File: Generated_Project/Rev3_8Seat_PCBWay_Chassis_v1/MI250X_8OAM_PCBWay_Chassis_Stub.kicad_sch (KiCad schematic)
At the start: 0 parts

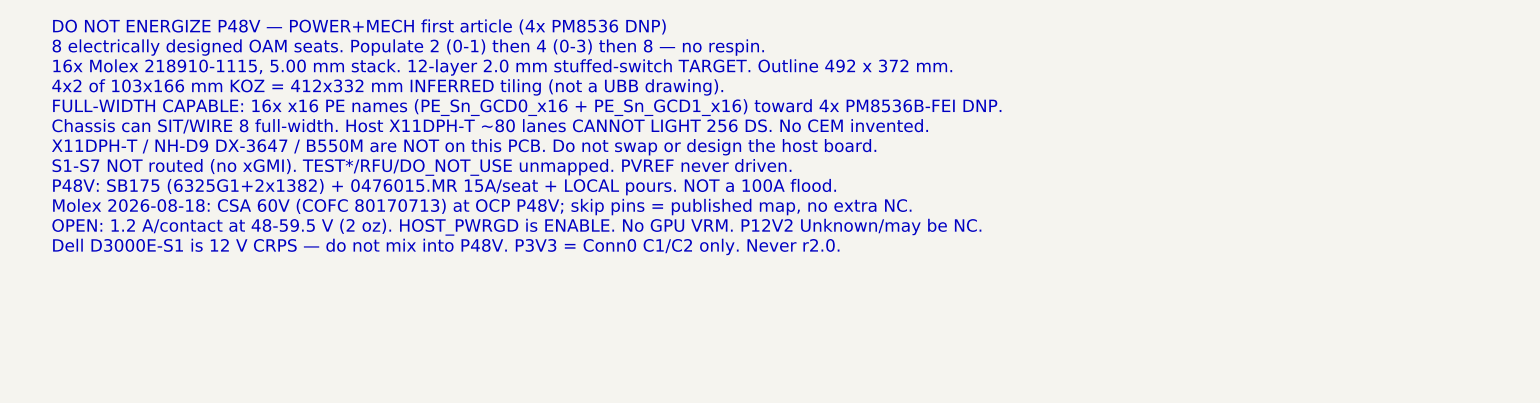
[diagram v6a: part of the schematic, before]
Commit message: Retarget Rev3 first article to seats 0-1 GCD0 x16 (2-module path).
Same 8-seat PCB. Without overlay, 2x MI250X means two modules can sit
and at most GCD0 on each can be named toward the host keepout (2 GCDs),
not 2x full-width (4 GCDs). Conn0 OCP PCIE_* is the only legal host PE.
No CEM/MCIO MPN. Do not energize P48V.

Co-authored-by: zivzancoeli-commits <zivzancoeli-commits@users.noreply.github.com>
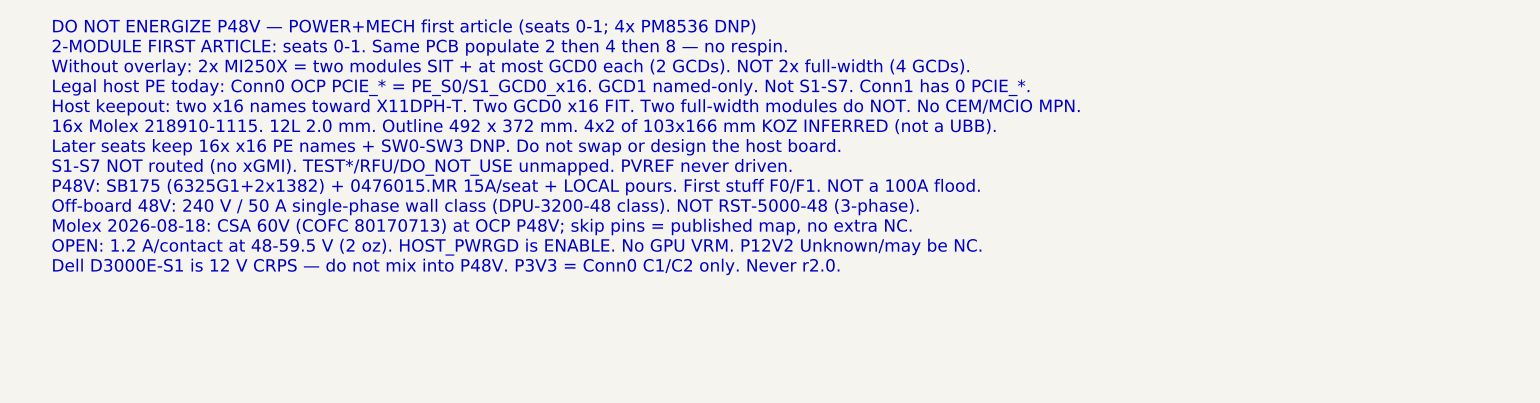
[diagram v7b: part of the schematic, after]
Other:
- note added: "DO NOT ENERGIZE P48V — POWER+MECH first article (seats 0-1; 4x PM8536 DNP) 2-MODULE FIRST ARTICLE: seats 0-1. Same PCB populate 2 then 4 then 8 — no respin. Without overlay: 2x MI250X = two modules SIT + at most GCD0 each (2 GCDs). NOT 2x full-width (4 GCDs). Legal host PE today: Conn0 OCP PCIE_* = PE_S0/S1_GCD0_x16. GCD1 named-only. Not S1-S7. Conn1 has 0 PCIE_*. Host keepout: two x16 names towa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"
- note removed: "DO NOT ENERGIZE P48V — POWER+MECH first article (4x PM8536 DNP) 8 electrically designed OAM seats. Populate 2 (0-1) then 4 (0-3) then 8 — no respin. 16x Molex 218910-1115, 5.00 mm stack. 12-layer 2.0 mm stuffed-switch TARGET. Outline 492 x 372 mm. 4x2 of 103x166 mm KOZ = 412x332 mm INFERRED tiling (not a UBB drawing). FULL-WIDTH CAPABLE: 16x x16 PE names (PE_Sn_GCD0_x16 + PE_Sn_GCD1_x16) toward 4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"
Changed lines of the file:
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@@
 		(rev "Rev3_8Seat_PCBWay_v1")
         (comment 1 "DO NOT ENERGIZE P48V. Molex 60V written 2026-08-18; 1.2A/contact OPEN. Skip-pin NC.")
-        (comment 2 "8 OAM seats. Host X11DPH-T is NOT on this PCB. Chassis full-width capable; host cannot light 256 DS. No CEM cable.")
+        (comment 2 "8 OAM seats. FIRST ARTICLE = seats 0-1 GCD0 x16. Host X11DPH-T is NOT on this PCB. No CEM cable.")
         (comment 3 "Pin names: OAM Pin map rev 1.0.xlsx — OCP generic, NOT AMD overlay")
         (comment 4 "r2.0 UNUSABLE. P3V3=Conn0 C1/C2. 12L 2.0mm stuffed-switch TARGET. 4x PM8536 DNP. Star-fed P48V.")
 	)
-	(text "DO NOT ENERGIZE P48V — POWER+MECH first article (4x PM8536 DNP)\n8 electrically designed OAM seats. Populate 2 (0-1) then 4 (0-3) then 8 — no respin.\n16x Molex 218910-1115, 5.00 mm stack. 12-layer 2.0 mm stuffed-switch TARGET. Outline 492 x 372 mm.\n4x2 of 103x166 mm KOZ = 412x332 mm INFERRED tiling (not a UBB drawing).\nFULL-WIDTH CAPABLE: 16x x16 PE names (PE_Sn_GCD0_x16 + PE_Sn_GCD1_x16) toward 4x PM8536B-FEI DNP.\nChassis can SIT/WIRE 8 full-width. Host X11DPH-T ~80 lanes CANNOT LIGHT 256 DS. No CEM invented.\nX11DPH-T / NH-D9 DX-3647 / B550M are NOT on this PCB. Do not swap or design the host board.\nS1-S7 NOT routed (no xGMI). TEST*/RFU/DO_NOT_USE unmapped. PVREF never driven.\nP48V: SB175 (6325G1+2x1382) + 0476015.MR 15A/seat + LOCAL pours. NOT a 100A flood.\nMolex 2026-08-18: CSA 60V (COFC 80170713) at OCP P48V; skip pins = published map, no extra NC.\nOPEN: 1.2 A/contact at 48-59.5 V (2 oz). HOST_PWRGD is ENABLE. No GPU VRM. P12V2 Unknown/may be NC.\nDell D3000E-S1 is 12 V CRPS — do not mix into P48V. P3V3 = Conn0 C1/C2 only. Never r2.0."
+	(text "DO NOT ENERGIZE P48V — POWER+MECH first article (seats 0-1; 4x PM8536 DNP)\n2-MODULE FIRST ARTICLE: seats 0-1. Same PCB populate 2 then 4 then 8 — no respin.\nWithout overlay: 2x MI250X = two modules SIT + at most GCD0 each (2 GCDs). NOT 2x full-width (4 GCDs).\nLegal host PE today: Conn0 OCP PCIE_* = PE_S0/S1_GCD0_x16. GCD1 named-only. Not S1-S7. Conn1 has 0 PCIE_*.\nHost keepout: two x16 names toward X11DPH-T. Two GCD0 x16 FIT. Two full-width modules do NOT. No CEM/MCIO MPN.\n16x Molex 218910-1115. 12L 2.0 mm. Outline 492 x 372 mm. 4x2 of 103x166 mm KOZ INFERRED (not a UBB).\nLater seats keep 16x x16 PE names + SW0-SW3 DNP. Do not swap or design the host board.\nS1-S7 NOT routed (no xGMI). TEST*/RFU/DO_NOT_USE unmapped. PVREF never driven.\nP48V: SB175 (6325G1+2x1382) + 0476015.MR 15A/seat + LOCAL pours. First stuff F0/F1. NOT a 100A flood.\nOff-board 48V: 240 V / 50 A single-phase wall class (DPU-3200-48 class). NOT RST-5000-48 (3-phase).\nMolex 2026-08-18: CSA 60V (COFC 80170713) at OCP P48V; skip pins = published map, no extra NC.\nOPEN: 1.2 A/contact at 48-59.5 V (2 oz). HOST_PWRGD is ENABLE. No GPU VRM. P12V2 Unknown/may be NC.\nDell D3000E-S1 is 12 V CRPS — do not mix into P48V. P3V3 = Conn0 C1/C2 only. Never r2.0."
 		(exclude_from_sim no)
 		(at 25.4 15.24 0)
@@
 		(instances
 			(project "MI250X_8OAM_PCBWay_Chassis_Stub"
-				(path "/55d1fb6f-3b8f-4a23-aee7-008dfc99f7b0"
+				(path "/02bc8d49-c633-48aa-a7e7-b32c4341abeb"
 					(page "2")
 				)
@@
 		(instances
 			(project "MI250X_8OAM_PCBWay_Chassis_Stub"
-				(path "/55d1fb6f-3b8f-4a23-aee7-008dfc99f7b0"
+				(path "/02bc8d49-c633-48aa-a7e7-b32c4341abeb"
 					(page "3")
 				)
@@
 		(instances
 			(project "MI250X_8OAM_PCBWay_Chassis_Stub"
-				(path "/55d1fb6f-3b8f-4a23-aee7-008dfc99f7b0"
+				(path "/02bc8d49-c633-48aa-a7e7-b32c4341abeb"
 					(page "4")
 				)
@@
 		(instances
 			(project "MI250X_8OAM_PCBWay_Chassis_Stub"
-				(path "/55d1fb6f-3b8f-4a23-aee7-008dfc99f7b0"
+				(path "/02bc8d49-c633-48aa-a7e7-b32c4341abeb"
 					(page "5")
 				)
@@
 		(instances
 			(project "MI250X_8OAM_PCBWay_Chassis_Stub"
-				(path "/55d1fb6f-3b8f-4a23-aee7-008dfc99f7b0"
+				(path "/02bc8d49-c633-48aa-a7e7-b32c4341abeb"
 					(page "6")
 				)
@@
 		(instances
 			(project "MI250X_8OAM_PCBWay_Chassis_Stub"
-				(path "/55d1fb6f-3b8f-4a23-aee7-008dfc99f7b0"
+				(path "/02bc8d49-c633-48aa-a7e7-b32c4341abeb"
 					(page "7")
 				)
@@
 		(instances
 			(project "MI250X_8OAM_PCBWay_Chassis_Stub"
-				(path "/55d1fb6f-3b8f-4a23-aee7-008dfc99f7b0"
+				(path "/02bc8d49-c633-48aa-a7e7-b32c4341abeb"
 					(page "8")
 				)
@@
 		(instances
 			(project "MI250X_8OAM_PCBWay_Chassis_Stub"
-				(path "/55d1fb6f-3b8f-4a23-aee7-008dfc99f7b0"
+				(path "/02bc8d49-c633-48aa-a7e7-b32c4341abeb"
 					(page "9")
 				)
@@
 		(instances
 			(project "MI250X_8OAM_PCBWay_Chassis_Stub"
-				(path "/55d1fb6f-3b8f-4a23-aee7-008dfc99f7b0"
+				(path "/02bc8d49-c633-48aa-a7e7-b32c4341abeb"
 					(page "10")
 				)
@@
 		(instances
 			(project "MI250X_8OAM_PCBWay_Chassis_Stub"
-				(path "/55d1fb6f-3b8f-4a23-aee7-008dfc99f7b0"
+				(path "/02bc8d49-c633-48aa-a7e7-b32c4341abeb"
 					(page "11")
 				)
@@
 		(instances
 			(project "MI250X_8OAM_PCBWay_Chassis_Stub"
-				(path "/55d1fb6f-3b8f-4a23-aee7-008dfc99f7b0"
+				(path "/02bc8d49-c633-48aa-a7e7-b32c4341abeb"
 					(page "12")
 				)
@@
 		(instances
 			(project "MI250X_8OAM_PCBWay_Chassis_Stub"
-				(path "/55d1fb6f-3b8f-4a23-aee7-008dfc99f7b0"
+				(path "/02bc8d49-c633-48aa-a7e7-b32c4341abeb"
 					(page "13")
 				)
@@
 		(instances
 			(project "MI250X_8OAM_PCBWay_Chassis_Stub"
-				(path "/55d1fb6f-3b8f-4a23-aee7-008dfc99f7b0"
+				(path "/02bc8d49-c633-48aa-a7e7-b32c4341abeb"
 					(page "14")
 				)

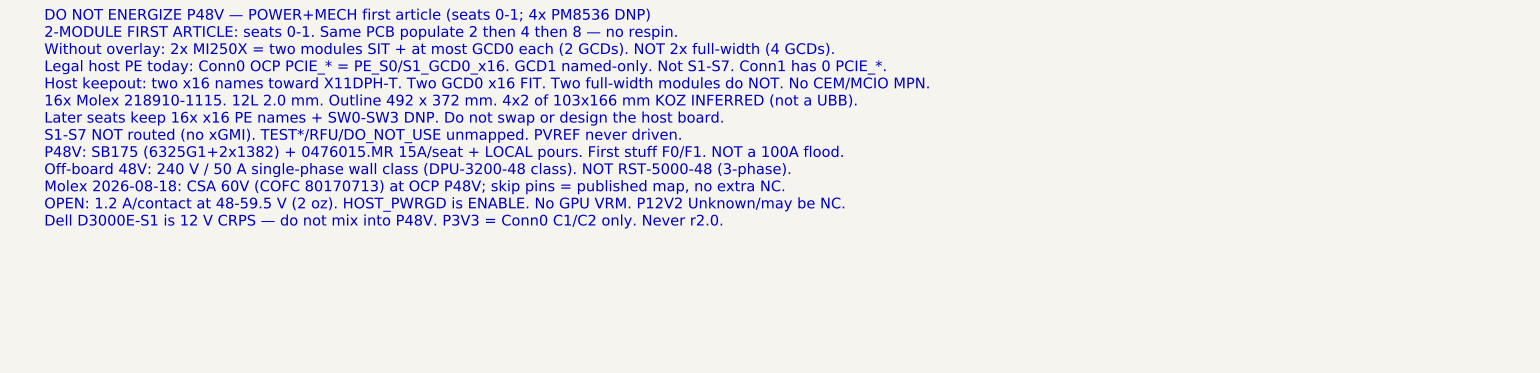
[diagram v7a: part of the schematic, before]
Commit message: Document an 8x full-width chassis CONCEPT (ideas only, not fab).
Sibling folder plus STATUS pointer. Comments-layer KiCad notes say
CONCEPT / DO NOT FABRICATE. No overlay, ball map, CEM/MCIO, r2.0, or
S1-S7 assignment. X11DPH-T cannot light 256 DS. Do not energize.
Do not upload to PCBWay.

Co-authored-by: zivzancoeli-commits <zivzancoeli-commits@users.noreply.github.com>
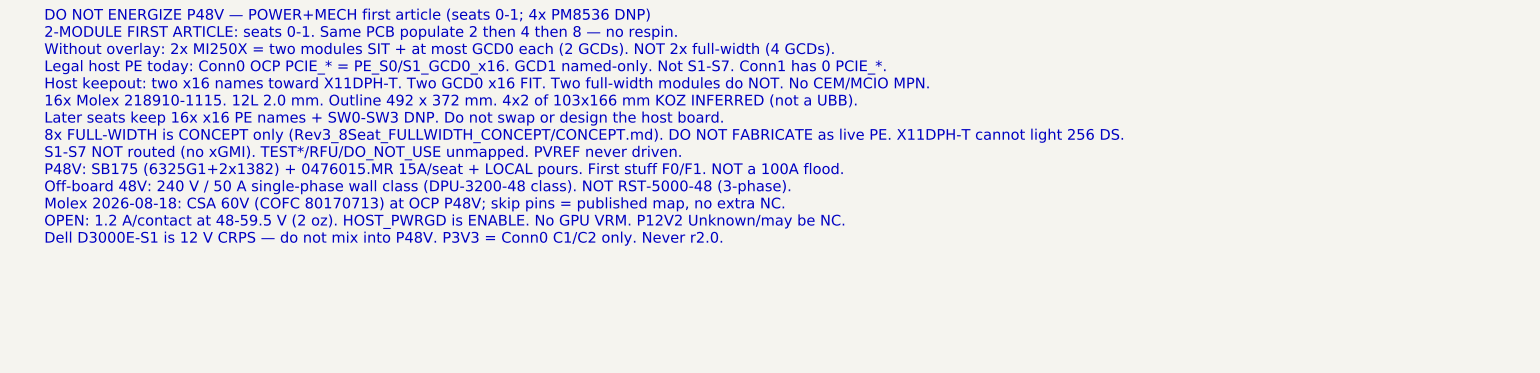
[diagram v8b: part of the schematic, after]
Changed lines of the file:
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@@
         (comment 4 "r2.0 UNUSABLE. P3V3=Conn0 C1/C2. 12L 2.0mm stuffed-switch TARGET. 4x PM8536 DNP. Star-fed P48V.")
 	)
-	(text "DO NOT ENERGIZE P48V — POWER+MECH first article (seats 0-1; 4x PM8536 DNP)\n2-MODULE FIRST ARTICLE: seats 0-1. Same PCB populate 2 then 4 then 8 — no respin.\nWithout overlay: 2x MI250X = two modules SIT + at most GCD0 each (2 GCDs). NOT 2x full-width (4 GCDs).\nLegal host PE today: Conn0 OCP PCIE_* = PE_S0/S1_GCD0_x16. GCD1 named-only. Not S1-S7. Conn1 has 0 PCIE_*.\nHost keepout: two x16 names toward X11DPH-T. Two GCD0 x16 FIT. Two full-width modules do NOT. No CEM/MCIO MPN.\n16x Molex 218910-1115. 12L 2.0 mm. Outline 492 x 372 mm. 4x2 of 103x166 mm KOZ INFERRED (not a UBB).\nLater seats keep 16x x16 PE names + SW0-SW3 DNP. Do not swap or design the host board.\nS1-S7 NOT routed (no xGMI). TEST*/RFU/DO_NOT_USE unmapped. PVREF never driven.\nP48V: SB175 (6325G1+2x1382) + 0476015.MR 15A/seat + LOCAL pours. First stuff F0/F1. NOT a 100A flood.\nOff-board 48V: 240 V / 50 A single-phase wall class (DPU-3200-48 class). NOT RST-5000-48 (3-phase).\nMolex 2026-08-18: CSA 60V (COFC 80170713) at OCP P48V; skip pins = published map, no extra NC.\nOPEN: 1.2 A/contact at 48-59.5 V (2 oz). HOST_PWRGD is ENABLE. No GPU VRM. P12V2 Unknown/may be NC.\nDell D3000E-S1 is 12 V CRPS — do not mix into P48V. P3V3 = Conn0 C1/C2 only. Never r2.0."
+	(text "DO NOT ENERGIZE P48V — POWER+MECH first article (seats 0-1; 4x PM8536 DNP)\n2-MODULE FIRST ARTICLE: seats 0-1. Same PCB populate 2 then 4 then 8 — no respin.\nWithout overlay: 2x MI250X = two modules SIT + at most GCD0 each (2 GCDs). NOT 2x full-width (4 GCDs).\nLegal host PE today: Conn0 OCP PCIE_* = PE_S0/S1_GCD0_x16. GCD1 named-only. Not S1-S7. Conn1 has 0 PCIE_*.\nHost keepout: two x16 names toward X11DPH-T. Two GCD0 x16 FIT. Two full-width modules do NOT. No CEM/MCIO MPN.\n16x Molex 218910-1115. 12L 2.0 mm. Outline 492 x 372 mm. 4x2 of 103x166 mm KOZ INFERRED (not a UBB).\nLater seats keep 16x x16 PE names + SW0-SW3 DNP. Do not swap or design the host board.\n8x FULL-WIDTH is CONCEPT only (Rev3_8Seat_FULLWIDTH_CONCEPT/CONCEPT.md). DO NOT FABRICATE as live PE. X11DPH-T cannot light 256 DS.\nS1-S7 NOT routed (no xGMI). TEST*/RFU/DO_NOT_USE unmapped. PVREF never driven.\nP48V: SB175 (6325G1+2x1382) + 0476015.MR 15A/seat + LOCAL pours. First stuff F0/F1. NOT a 100A flood.\nOff-board 48V: 240 V / 50 A single-phase wall class (DPU-3200-48 class). NOT RST-5000-48 (3-phase).\nMolex 2026-08-18: CSA 60V (COFC 80170713) at OCP P48V; skip pins = published map, no extra NC.\nOPEN: 1.2 A/contact at 48-59.5 V (2 oz). HOST_PWRGD is ENABLE. No GPU VRM. P12V2 Unknown/may be NC.\nDell D3000E-S1 is 12 V CRPS — do not mix into P48V. P3V3 = Conn0 C1/C2 only. Never r2.0."
 		(exclude_from_sim no)
 		(at 25.4 15.24 0)
